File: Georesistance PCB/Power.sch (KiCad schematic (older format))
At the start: 24 parts, among them Q7 TIP122, U10 AP2127N-2.5, U11 LM350_TO220, U8 LM2776, U9 LM337L_TO92

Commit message: Actually fixed the schematic
Hopefully for the last time
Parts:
- renumbered Q7 to Q8, U11 to U10, U8 to U7, U9 to U8, U10 to U9
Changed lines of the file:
@@
 P 1550 1950
 AR Path="/61409444/614DD5E2" Ref="U?"  Part="1"
-AR Path="/614B3A1B/614DD5E2" Ref="U8"  Part="1"
-F 0 "U8" H 1994 1946 50  0000 L CNN
+AR Path="/614B3A1B/614DD5E2" Ref="U7"  Part="1"
+F 0 "U7" H 1994 1946 50  0000 L CNN
 F 1 "LM2776" H 1994 1855 50  0000 L CNN
 F 2 "Package_TO_SOT_SMD:SOT-23-6" H 1600 1600 50  0001 L CNN
@@
 P 7850 1650
 AR Path="/61409444/614DD680" Ref="U?"  Part="1"
-AR Path="/614B3A1B/614DD680" Ref="U11"  Part="1"
-F 0 "U11" H 7850 1892 50  0000 C CNN
+AR Path="/614B3A1B/614DD680" Ref="U10"  Part="1"
+F 0 "U10" H 7850 1892 50  0000 C CNN
 F 1 "LM350_TO220" H 7850 1801 50  0000 C CNN
 F 2 "Package_TO_SOT_THT:TO-220-3_Vertical" H 7850 1900 50  0001 C CIN
@@
 P 6700 1750
 AR Path="/61409444/614DD6BE" Ref="Q?"  Part="1"
-AR Path="/614B3A1B/614DD6BE" Ref="Q7"  Part="1"
-F 0 "Q7" V 7044 1750 50  0000 C CNN
+AR Path="/614B3A1B/614DD6BE" Ref="Q8"  Part="1"
+F 0 "Q8" V 7044 1750 50  0000 C CNN
 F 1 "TIP122" V 6953 1750 50  0000 C CNN
 F 2 "Package_TO_SOT_THT:TO-220-3_Vertical" H 6900 1675 50  0001 L CIN
@@
 P 1600 4600
 AR Path="/61409444/614DD6C4" Ref="U?"  Part="1"
-AR Path="/614B3A1B/614DD6C4" Ref="U9"  Part="1"
-F 0 "U9" H 1600 4451 50  0000 C CNN
+AR Path="/614B3A1B/614DD6C4" Ref="U8"  Part="1"
+F 0 "U8" H 1600 4451 50  0000 C CNN
 F 1 "LM337L_TO92" H 1600 4360 50  0000 C CNN
 F 2 "Package_TO_SOT_THT:TO-92_Inline" H 1600 4400 50  0001 C CIN
@@
 P 1750 3400
 AR Path="/61409444/614DD6EF" Ref="U?"  Part="1"
-AR Path="/614B3A1B/614DD6EF" Ref="U10"  Part="1"
-F 0 "U10" H 1750 3642 50  0000 C CNN
+AR Path="/614B3A1B/614DD6EF" Ref="U9"  Part="1"
+F 0 "U9" H 1750 3642 50  0000 C CNN
 F 1 "AP2127N-2.5" H 1750 3551 50  0000 C CNN
 F 2 "Package_TO_SOT_SMD:SOT-23" H 1750 3625 50  0001 C CIN

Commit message: edited the PCB a little bit
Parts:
- D1, D2: value D -> DSR1M
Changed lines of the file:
@@
 AR Path="/614B3A1B/614DD63F" Ref="D2"  Part="1"
 F 0 "D2" H 8850 2017 50  0000 C CNN
-F 1 "D" H 8850 1926 50  0000 C CNN
+F 1 "DSR1M" H 8850 1926 50  0000 C CNN
 F 2 "Diode_SMD:D_SOD-123" H 8850 1800 50  0001 C CNN
 F 3 "~" H 8850 1800 50  0001 C CNN
@@
 AR Path="/614B3A1B/614DD645" Ref="D1"  Part="1"
 F 0 "D1" H 7800 1467 50  0000 C CNN
-F 1 "D" H 7800 1376 50  0000 C CNN
+F 1 "DSR1M" H 7800 1376 50  0000 C CNN
 F 2 "Diode_SMD:D_SOD-123" H 7800 1250 50  0001 C CNN
 F 3 "~" H 7800 1250 50  0001 C CNN

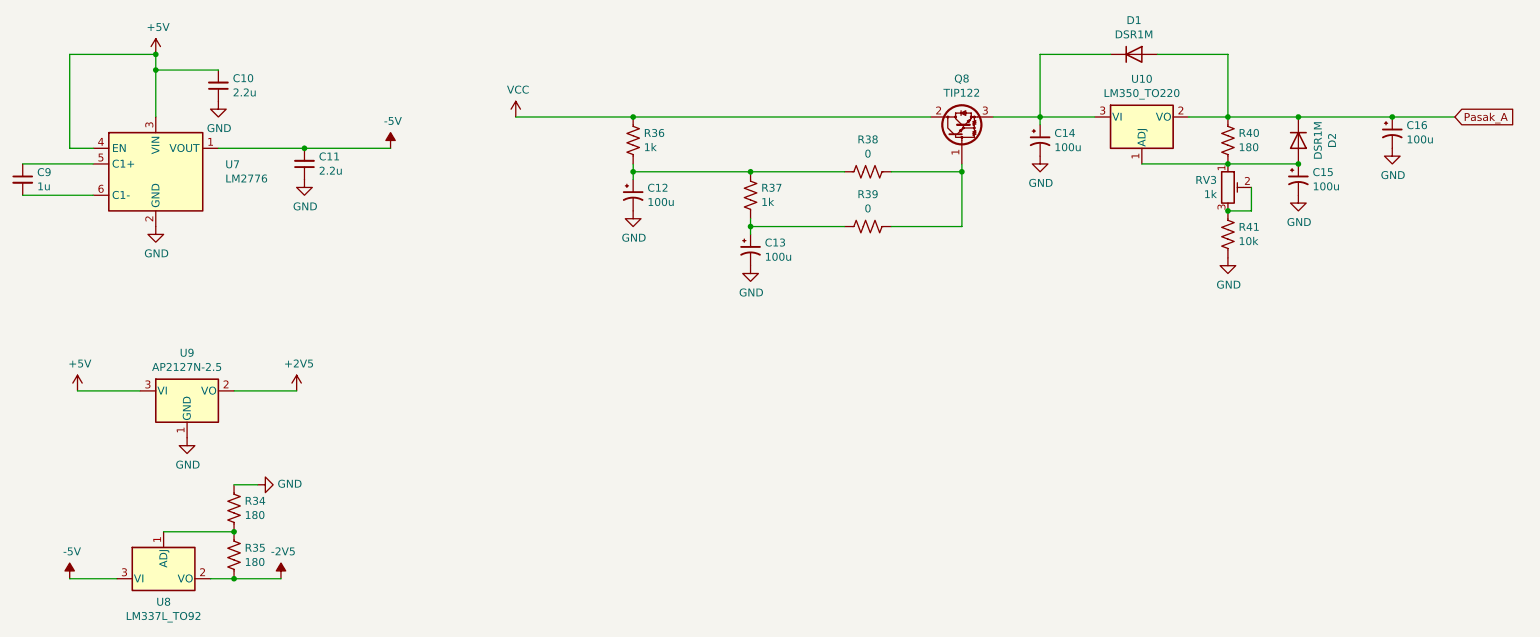
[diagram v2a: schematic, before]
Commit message: Added the PCB layout and simplified schematic
deleted jumper, and fixed misconnection
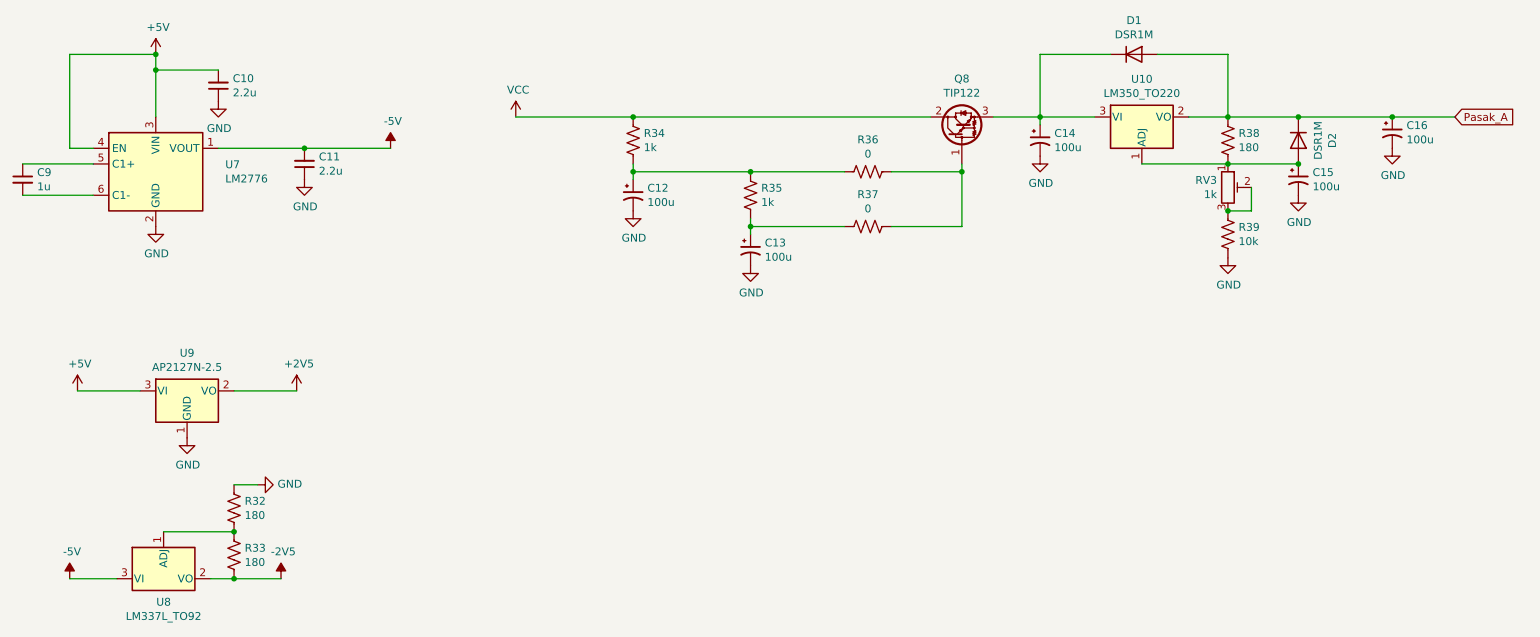
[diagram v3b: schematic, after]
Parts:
- renumbered R34 to R32, R35 to R33, R36 to R34, R37 to R35, R38 to R36, R39 to R37, R40 to R38, R41 to R39
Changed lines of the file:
@@
 P 1550 1250
 AR Path="/61409444/614DD5E8" Ref="#PWR?"  Part="1"
-AR Path="/614B3A1B/614DD5E8" Ref="#PWR048"  Part="1"
-F 0 "#PWR048" H 1550 1100 50  0001 C CNN
+AR Path="/614B3A1B/614DD5E8" Ref="#PWR047"  Part="1"
+F 0 "#PWR047" H 1550 1100 50  0001 C CNN
 F 1 "+5V" H 1565 1423 50  0000 C CNN
 F 2 "" H 1550 1250 50  0001 C CNN
@@
 P 1950 1550
 AR Path="/61409444/614DD5F6" Ref="#PWR?"  Part="1"
-AR Path="/614B3A1B/614DD5F6" Ref="#PWR051"  Part="1"
-F 0 "#PWR051" H 1950 1300 50  0001 C CNN
+AR Path="/614B3A1B/614DD5F6" Ref="#PWR050"  Part="1"
+F 0 "#PWR050" H 1950 1300 50  0001 C CNN
 F 1 "GND" H 1955 1377 50  0000 C CNN
 F 2 "" H 1950 1550 50  0001 C CNN
@@
 P 2500 2050
 AR Path="/61409444/614DD610" Ref="#PWR?"  Part="1"
-AR Path="/614B3A1B/614DD610" Ref="#PWR055"  Part="1"
-F 0 "#PWR055" H 2500 1800 50  0001 C CNN
+AR Path="/614B3A1B/614DD610" Ref="#PWR054"  Part="1"
+F 0 "#PWR054" H 2500 1800 50  0001 C CNN
 F 1 "GND" H 2505 1877 50  0000 C CNN
 F 2 "" H 2500 2050 50  0001 C CNN
@@
 P 3050 1850
 AR Path="/61409444/614DD617" Ref="#PWR?"  Part="1"
-AR Path="/614B3A1B/614DD617" Ref="#PWR056"  Part="1"
-F 0 "#PWR056" H 3050 1950 50  0001 C CNN
+AR Path="/614B3A1B/614DD617" Ref="#PWR055"  Part="1"
+F 0 "#PWR055" H 3050 1950 50  0001 C CNN
 F 1 "-5V" H 3065 2023 50  0000 C CNN
 F 2 "" H 3050 1850 50  0001 C CNN
@@
 P 8400 1800
 AR Path="/61409444/614DD62F" Ref="R?"  Part="1"
-AR Path="/614B3A1B/614DD62F" Ref="R40"  Part="1"
-F 0 "R40" H 8468 1846 50  0000 L CNN
+AR Path="/614B3A1B/614DD62F" Ref="R38"  Part="1"
+F 0 "R38" H 8468 1846 50  0000 L CNN
 F 1 "180" H 8468 1755 50  0000 L CNN
 F 2 "Resistor_THT:R_Axial_DIN0207_L6.3mm_D2.5mm_P7.62mm_Horizontal" V 8440 1790 50  0001 C CNN
@@
 P 8850 2150
 AR Path="/61409444/614DD64B" Ref="#PWR?"  Part="1"
-AR Path="/614B3A1B/614DD64B" Ref="#PWR062"  Part="1"
-F 0 "#PWR062" H 8850 1900 50  0001 C CNN
+AR Path="/614B3A1B/614DD64B" Ref="#PWR061"  Part="1"
+F 0 "#PWR061" H 8850 1900 50  0001 C CNN
 F 1 "GND" H 8855 1977 50  0000 C CNN
 F 2 "" H 8850 2150 50  0001 C CNN
@@
 P 9450 1850
 AR Path="/61409444/614DD657" Ref="#PWR?"  Part="1"
-AR Path="/614B3A1B/614DD657" Ref="#PWR063"  Part="1"
-F 0 "#PWR063" H 9450 1600 50  0001 C CNN
+AR Path="/614B3A1B/614DD657" Ref="#PWR062"  Part="1"
+F 0 "#PWR062" H 9450 1600 50  0001 C CNN
 F 1 "GND" H 9455 1677 50  0000 C CNN
 F 2 "" H 9450 1850 50  0001 C CNN
@@
 P 8400 2550
 AR Path="/61409444/614DD663" Ref="#PWR?"  Part="1"
-AR Path="/614B3A1B/614DD663" Ref="#PWR061"  Part="1"
-F 0 "#PWR061" H 8400 2300 50  0001 C CNN
+AR Path="/614B3A1B/614DD663" Ref="#PWR060"  Part="1"
+F 0 "#PWR060" H 8400 2300 50  0001 C CNN
 F 1 "GND" H 8405 2377 50  0000 C CNN
 F 2 "" H 8400 2550 50  0001 C CNN
@@
 P 8400 2400
 AR Path="/61409444/614DD669" Ref="R?"  Part="1"
-AR Path="/614B3A1B/614DD669" Ref="R41"  Part="1"
-F 0 "R41" H 8468 2446 50  0000 L CNN
+AR Path="/614B3A1B/614DD669" Ref="R39"  Part="1"
+F 0 "R39" H 8468 2446 50  0000 L CNN
 F 1 "10k" H 8468 2355 50  0000 L CNN
 F 2 "Resistor_THT:R_Axial_DIN0207_L6.3mm_D2.5mm_P7.62mm_Horizontal" V 8440 2390 50  0001 C CNN
@@
 P 7200 1900
 AR Path="/61409444/614DD674" Ref="#PWR?"  Part="1"
-AR Path="/614B3A1B/614DD674" Ref="#PWR060"  Part="1"
-F 0 "#PWR060" H 7200 1650 50  0001 C CNN
+AR Path="/614B3A1B/614DD674" Ref="#PWR059"  Part="1"
+F 0 "#PWR059" H 7200 1650 50  0001 C CNN
 F 1 "GND" H 7205 1727 50  0000 C CNN
 F 2 "" H 7200 1900 50  0001 C CNN
@@
 P 5350 2150
 AR Path="/61409444/614DD69E" Ref="R?"  Part="1"
-AR Path="/614B3A1B/614DD69E" Ref="R37"  Part="1"
-F 0 "R37" H 5418 2196 50  0000 L CNN
+AR Path="/614B3A1B/614DD69E" Ref="R35"  Part="1"
+F 0 "R35" H 5418 2196 50  0000 L CNN
 F 1 "1k" H 5418 2105 50  0000 L CNN
 F 2 "Resistor_THT:R_Axial_DIN0207_L6.3mm_D2.5mm_P7.62mm_Horizontal" V 5390 2140 50  0001 C CNN
@@
 P 4600 2250
 AR Path="/61409444/614DD6A4" Ref="#PWR?"  Part="1"
-AR Path="/614B3A1B/614DD6A4" Ref="#PWR058"  Part="1"
-F 0 "#PWR058" H 4600 2000 50  0001 C CNN
+AR Path="/614B3A1B/614DD6A4" Ref="#PWR057"  Part="1"
+F 0 "#PWR057" H 4600 2000 50  0001 C CNN
 F 1 "GND" H 4605 2077 50  0000 C CNN
 F 2 "" H 4600 2250 50  0001 C CNN
@@
 P 4600 1800
 AR Path="/61409444/614DD6B2" Ref="R?"  Part="1"
-AR Path="/614B3A1B/614DD6B2" Ref="R36"  Part="1"
-F 0 "R36" H 4668 1846 50  0000 L CNN
+AR Path="/614B3A1B/614DD6B2" Ref="R34"  Part="1"
+F 0 "R34" H 4668 1846 50  0000 L CNN
 F 1 "1k" H 4668 1755 50  0000 L CNN
 F 2 "Resistor_THT:R_Axial_DIN0207_L6.3mm_D2.5mm_P7.62mm_Horizontal" V 4640 1790 50  0001 C CNN
@@
 P 3850 1650
 AR Path="/61409444/614DD6B8" Ref="#PWR?"  Part="1"
-AR Path="/614B3A1B/614DD6B8" Ref="#PWR057"  Part="1"
-F 0 "#PWR057" H 3850 1500 50  0001 C CNN
+AR Path="/614B3A1B/614DD6B8" Ref="#PWR056"  Part="1"
+F 0 "#PWR056" H 3850 1500 50  0001 C CNN
 F 1 "VCC" H 3865 1823 50  0000 C CNN
 F 2 "" H 3850 1650 50  0001 C CNN
@@
 P 1000 4600
 AR Path="/61409444/614DD6CA" Ref="#PWR?"  Part="1"
-AR Path="/614B3A1B/614DD6CA" Ref="#PWR046"  Part="1"
-F 0 "#PWR046" H 1000 4700 50  0001 C CNN
+AR Path="/614B3A1B/614DD6CA" Ref="#PWR045"  Part="1"
+F 0 "#PWR045" H 1000 4700 50  0001 C CNN
 F 1 "-5V" H 1015 4773 50  0000 C CNN
 F 2 "" H 1000 4600 50  0001 C CNN
@@
 P 2350 4600
 AR Path="/61409444/614DD6D1" Ref="#PWR?"  Part="1"
-AR Path="/614B3A1B/614DD6D1" Ref="#PWR053"  Part="1"
-F 0 "#PWR053" H 2350 4700 50  0001 C CNN
+AR Path="/614B3A1B/614DD6D1" Ref="#PWR052"  Part="1"
+F 0 "#PWR052" H 2350 4700 50  0001 C CNN
 F 1 "-2V5" H 2365 4773 50  0000 C CNN
 F 2 "" H 2350 4600 50  0001 C CNN
@@
 P 2050 4450
 AR Path="/61409444/614DD6D8" Ref="R?"  Part="1"
-AR Path="/614B3A1B/614DD6D8" Ref="R35"  Part="1"
-F 0 "R35" H 2118 4496 50  0000 L CNN
+AR Path="/614B3A1B/614DD6D8" Ref="R33"  Part="1"
+F 0 "R33" H 2118 4496 50  0000 L CNN
 F 1 "180" H 2118 4405 50  0000 L CNN
 F 2 "Resistor_THT:R_Axial_DIN0207_L6.3mm_D2.5mm_P7.62mm_Horizontal" V 2090 4440 50  0001 C CNN
@@
 P 2050 4150
 AR Path="/61409444/614DD6E0" Ref="R?"  Part="1"
-AR Path="/614B3A1B/614DD6E0" Ref="R34"  Part="1"
-F 0 "R34" H 2118 4196 50  0000 L CNN
+AR Path="/614B3A1B/614DD6E0" Ref="R32"  Part="1"
+F 0 "R32" H 2118 4196 50  0000 L CNN
 F 1 "180" H 2118 4105 50  0000 L CNN
 F 2 "Resistor_THT:R_Axial_DIN0207_L6.3mm_D2.5mm_P7.62mm_Horizontal" V 2090 4140 50  0001 C CNN
@@
 P 2200 4000
 AR Path="/61409444/614DD6E8" Ref="#PWR?"  Part="1"
-AR Path="/614B3A1B/614DD6E8" Ref="#PWR052"  Part="1"
-F 0 "#PWR052" H 2200 3750 50  0001 C CNN
+AR Path="/614B3A1B/614DD6E8" Ref="#PWR051"  Part="1"
+F 0 "#PWR051" H 2200 3750 50  0001 C CNN
 F 1 "GND" V 2205 3872 50  0000 R CNN
 F 2 "" H 2200 4000 50  0001 C CNN
@@
 P 1050 3400
 AR Path="/61409444/614DD6F5" Ref="#PWR?"  Part="1"
-AR Path="/614B3A1B/614DD6F5" Ref="#PWR047"  Part="1"
-F 0 "#PWR047" H 1050 3250 50  0001 C CNN
+AR Path="/614B3A1B/614DD6F5" Ref="#PWR046"  Part="1"
+F 0 "#PWR046" H 1050 3250 50  0001 C CNN
 F 1 "+5V" H 1065 3573 50  0000 C CNN
 F 2 "" H 1050 3400 50  0001 C CNN
@@
 P 1750 3700
 AR Path="/61409444/614DD6FC" Ref="#PWR?"  Part="1"
-AR Path="/614B3A1B/614DD6FC" Ref="#PWR050"  Part="1"
-F 0 "#PWR050" H 1750 3450 50  0001 C CNN
+AR Path="/614B3A1B/614DD6FC" Ref="#PWR049"  Part="1"
+F 0 "#PWR049" H 1750 3450 50  0001 C CNN
 F 1 "GND" H 1755 3527 50  0000 C CNN
 F 2 "" H 1750 3700 50  0001 C CNN
@@
 P 2450 3400
 AR Path="/61409444/614DD702" Ref="#PWR?"  Part="1"
-AR Path="/614B3A1B/614DD702" Ref="#PWR054"  Part="1"
-F 0 "#PWR054" H 2450 3250 50  0001 C CNN
+AR Path="/614B3A1B/614DD702" Ref="#PWR053"  Part="1"
+F 0 "#PWR053" H 2450 3250 50  0001 C CNN
 F 1 "+2V5" H 2465 3573 50  0000 C CNN
 F 2 "" H 2450 3400 50  0001 C CNN
@@
 P 1550 2350
 AR Path="/61409444/614DD709" Ref="#PWR?"  Part="1"
-AR Path="/614B3A1B/614DD709" Ref="#PWR049"  Part="1"
-F 0 "#PWR049" H 1550 2100 50  0001 C CNN
+AR Path="/614B3A1B/614DD709" Ref="#PWR048"  Part="1"
+F 0 "#PWR048" H 1550 2100 50  0001 C CNN
 F 1 "GND" H 1555 2177 50  0000 C CNN
 F 2 "" H 1550 2350 50  0001 C CNN
@@
 P 5350 2600
 AR Path="/61409444/614DD716" Ref="#PWR?"  Part="1"
-AR Path="/614B3A1B/614DD716" Ref="#PWR059"  Part="1"
-F 0 "#PWR059" H 5350 2350 50  0001 C CNN
+AR Path="/614B3A1B/614DD716" Ref="#PWR058"  Part="1"
+F 0 "#PWR058" H 5350 2350 50  0001 C CNN
 F 1 "GND" H 5355 2427 50  0000 C CNN
 F 2 "" H 5350 2600 50  0001 C CNN
@@
 	5350 2350 5350 2400
 $Comp
-L Device:R_US R38
+L Device:R_US R36
 U 1 1 615D82EC
 P 6100 2000
-F 0 "R38" V 5895 2000 50  0000 C CNN
+F 0 "R36" V 5895 2000 50  0000 C CNN
 F 1 "0" V 5986 2000 50  0000 C CNN
 F 2 "Resistor_SMD:R_0402_1005Metric_Pad0.72x0.64mm_HandSolder" V 6140 1990 50  0001 C CNN
@@
 $EndComp
 $Comp
-L Device:R_US R39
+L Device:R_US R37
 U 1 1 615D9CB1
 P 6100 2350
-F 0 "R39" V 6305 2350 50  0000 C CNN
+F 0 "R37" V 6305 2350 50  0000 C CNN
 F 1 "0" V 6214 2350 50  0000 C CNN
 F 2 "Resistor_SMD:R_0402_1005Metric_Pad0.72x0.64mm_HandSolder" V 6140 2340 50  0001 C CNN

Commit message: added things
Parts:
- removed C10, C11: 2.2u, Capacitor_SMD:C_0402_1005Metric_Pad0.74x0.62mm_HandSolder, symbol Device:C_Small
- removed C9: 1u, Capacitor_SMD:C_0402_1005Metric_Pad0.74x0.62mm_HandSolder, symbol Device:C_Small
- removed R32, R33: 180, Resistor_THT:R_Axial_DIN0207_L6.3mm_D2.5mm_P7.62mm_Horizontal, symbol Device:R_US
- removed U7: LM2776, Package_TO_SOT_SMD:SOT-23-6, symbol Regulator_SwitchedCapacitor:LM2776
- removed U8: LM337L_TO92, Package_TO_SOT_THT:TO-92_Inline, symbol Regulator_Linear:LM337L_TO92
- removed U9: AP2127N-2.5, Package_TO_SOT_SMD:SOT-23, symbol Regulator_Linear:AP2127N-2.5
